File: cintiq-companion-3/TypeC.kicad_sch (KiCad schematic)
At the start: 22 parts, among them J7 USBC_Host, J8 USBC_Input

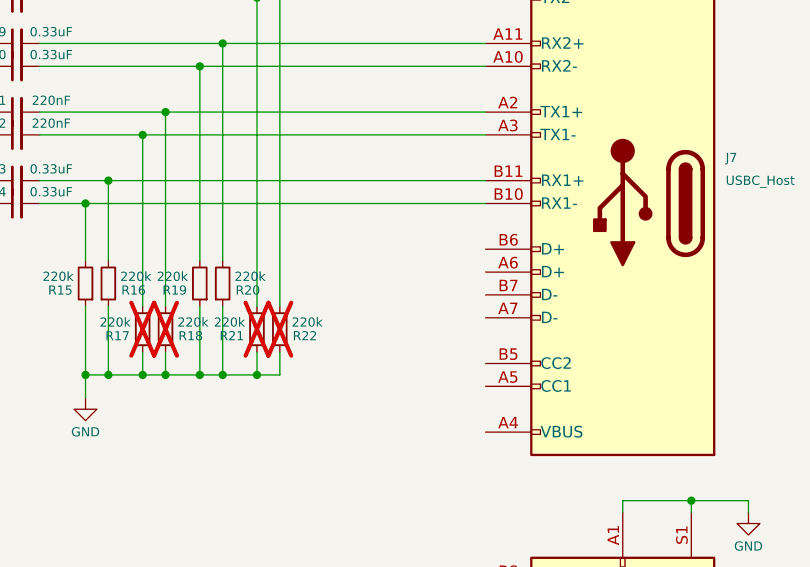
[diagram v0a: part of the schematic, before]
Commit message: flipped b-key lane order and added usb-c ports
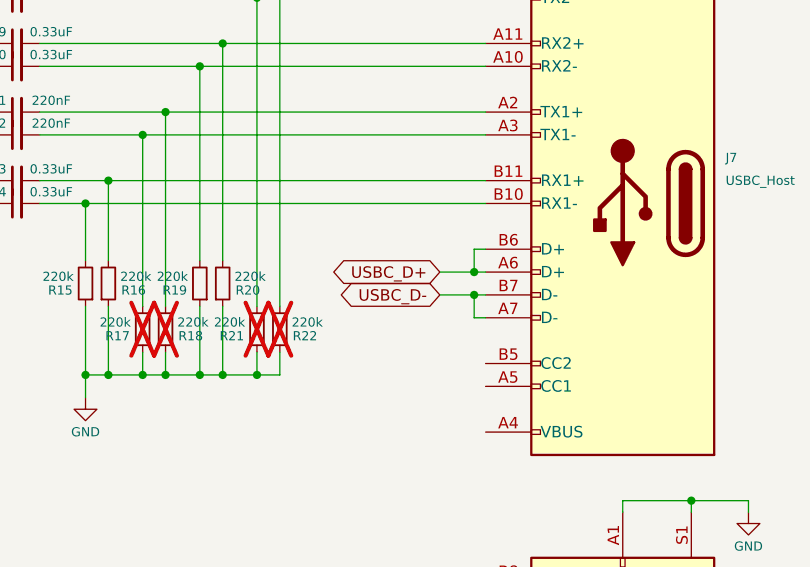
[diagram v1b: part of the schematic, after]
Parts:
- C27, C28, C29, C30, C31, C32, C33, C34: footprint Capacitor_SMD:C_0402_1005Metric -> Capacitor_SMD:C_0201_0603Metric
- R13, R14: footprint (none) -> Resistor_SMD:R_0402_1005Metric
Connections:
- net USBC_D+: now reaches J7.A6 (D+)
- net USBC_D+: now also J7.B6 (D+)
- net USBC_D-: now reaches J7.A7 (D-)
- net USBC_D-: now also J7.B7 (D-)
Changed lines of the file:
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@@
+	)
+	(junction
+		(at 245.11 67.31)
+		(diameter 0)
+		(color 0 0 0 0)
 	)
 	(junction
@@
 	)
 	(junction
+		(at 245.11 69.85)
+		(diameter 0)
+		(color 0 0 0 0)
+	)
+	(junction
 		(at 217.17 78.74)
 		(diameter 0)
@@
 	(wire
 		(pts
+			(xy 246.38 69.85) (xy 245.11 69.85)
+		)
+		(stroke
+			(width 0)
+			(type default)
+		)
+	)
+	(wire
+		(pts
 			(xy 201.93 78.74) (xy 204.47 78.74)
 		)
@@
 	(wire
 		(pts
+			(xy 245.11 67.31) (xy 246.38 67.31)
+		)
+		(stroke
+			(width 0)
+			(type default)
+		)
+	)
+	(wire
+		(pts
 			(xy 210.82 49.53) (xy 246.38 49.53)
 		)
@@
 	(wire
 		(pts
+			(xy 245.11 72.39) (xy 246.38 72.39)
+		)
+		(stroke
+			(width 0)
+			(type default)
+		)
+	)
+	(wire
+		(pts
+			(xy 245.11 64.77) (xy 245.11 67.31)
+		)
+		(stroke
+			(width 0)
+			(type default)
+		)
+	)
+	(wire
+		(pts
 			(xy 217.17 71.12) (xy 217.17 78.74)
 		)
@@
 	(wire
 		(pts
+			(xy 241.3 69.85) (xy 245.11 69.85)
+		)
+		(stroke
+			(width 0)
+			(type default)
+		)
+	)
+	(wire
+		(pts
 			(xy 198.12 22.86) (xy 209.55 22.86)
 		)
@@
 	(wire
 		(pts
+			(xy 245.11 69.85) (xy 245.11 72.39)
+		)
+		(stroke
+			(width 0)
+			(type default)
+		)
+	)
+	(wire
+		(pts
 			(xy 196.85 44.45) (xy 214.63 44.45)
 		)
@@
 	(wire
 		(pts
+			(xy 246.38 64.77) (xy 245.11 64.77)
+		)
+		(stroke
+			(width 0)
+			(type default)
+		)
+	)
+	(wire
+		(pts
 			(xy 196.85 52.07) (xy 208.28 52.07)
 		)
@@
 		(pts
 			(xy 217.17 66.04) (xy 217.17 41.91)
+		)
+		(stroke
+			(width 0)
+			(type default)
+		)
+	)
+	(wire
+		(pts
+			(xy 241.3 67.31) (xy 245.11 67.31)
 		)
 		(stroke
@@
 		)
 	)
+	(global_label "USBC_D+"
+		(shape bidirectional)
+		(at 241.3 67.31 180)
+		(fields_autoplaced yes)
+		(effects
+			(font
+				(size 1.27 1.27)
+			)
+			(justify right)
+		)
+		(property "Intersheetrefs" "${INTERSHEET_REFS}"
+			(at 228.3135 67.31 0)
+			(effects
+				(font
+					(size 1.27 1.27)
+				)
+				(justify right)
+				(hide yes)
+			)
+		)
+	)
 	(global_label "TCP1_DDC_SCL"
 		(shape input)
@@
 					(size 1.27 1.27)
 				)
+				(hide yes)
+			)
+		)
+	)
+	(global_label "USBC_D-"
+		(shape bidirectional)
+		(at 241.3 69.85 180)
+		(fields_autoplaced yes)
+		(effects
+			(font
+				(size 1.27 1.27)
+			)
+			(justify right)
+		)
+		(property "Intersheetrefs" "${INTERSHEET_REFS}"
+			(at 228.3135 69.85 0)
+			(effects
+				(font
+					(size 1.27 1.27)
+				)
+				(justify right)
 				(hide yes)
 			)
@@
 			)
 		)
-		(property "Footprint" ""
+		(property "Footprint" "Resistor_SMD:R_0402_1005Metric"
 			(at 212.09 20.32 0)
 			(effects
@@
 			)
 		)
-		(property "Footprint" "Capacitor_SMD:C_0402_1005Metric"
+		(property "Footprint" "Capacitor_SMD:C_0201_0603Metric"
 			(at 194.31 34.29 0)
 			(effects
@@
 			)
 		)
-		(property "Footprint" ""
+		(property "Footprint" "Resistor_SMD:R_0402_1005Metric"
 			(at 212.09 22.86 0)
 			(effects
@@
 			)
 		)
-		(property "Footprint" "Capacitor_SMD:C_0402_1005Metric"
+		(property "Footprint" "Capacitor_SMD:C_0201_0603Metric"
 			(at 194.31 41.91 0)
 			(effects
@@
 			)
 		)
-		(property "Footprint" "Capacitor_SMD:C_0402_1005Metric"
+		(property "Footprint" "Capacitor_SMD:C_0201_0603Metric"
 			(at 194.31 52.07 0)
 			(effects
@@
 			)
 		)
-		(property "Footprint" "Capacitor_SMD:C_0402_1005Metric"
+		(property "Footprint" "Capacitor_SMD:C_0201_0603Metric"
 			(at 194.31 57.15 0)
 			(effects
@@
 			)
 		)
-		(property "Footprint" "Capacitor_SMD:C_0402_1005Metric"
+		(property "Footprint" "Capacitor_SMD:C_0201_0603Metric"
 			(at 194.31 36.83 0)
 			(effects
@@
 			)
 		)
-		(property "Footprint" "Capacitor_SMD:C_0402_1005Metric"
+		(property "Footprint" "Capacitor_SMD:C_0201_0603Metric"
 			(at 194.31 49.53 0)
 			(effects
@@
 			)
 		)
-		(property "Footprint" "Capacitor_SMD:C_0402_1005Metric"
+		(property "Footprint" "Capacitor_SMD:C_0201_0603Metric"
 			(at 194.31 59.69 0)
 			(effects
@@
 			)
 		)
-		(property "Footprint" "Capacitor_SMD:C_0402_1005Metric"
+		(property "Footprint" "Capacitor_SMD:C_0201_0603Metric"
 			(at 194.31 44.45 0)
 			(effects

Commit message: unflipped m-key polarity for sata
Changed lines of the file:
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@@
 (kicad_sch
-	(version 20231120)
+	(version 20250114)
 	(generator "eeschema")
-	(generator_version "8.0")
+	(generator_version "9.0")
 	(paper "A4")
 	(junction
